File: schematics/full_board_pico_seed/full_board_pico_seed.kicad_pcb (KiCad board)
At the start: 4 copper layers, 128.3 x 74.9 mm, 135 parts, among them J1 XLR3, J10 Conn_02x20_Odd_Even, J2 Conn_01x02_Male, J3 Aux In, J4 Conn_01x02_Pin, J5 Conn_02x03_Odd_Even, J6 Conn_01x03_Female, J7 XLR3, J8 XLR3, J9 Conn_01x03, P0 25k, P1 25k, P2 25k, SW1 Stompbutton 1, SW2 Stompbutton 2, SW3 Stompbutton 3, SW4 Enter, SW5 Exit, U10 LM4881M/NOPB, U12 128X64 OLED Display, U14 AP63205WU, U2 PCM3060PWR, U3 LM1117DT-5.0, U4 OPA134, U5 ATmega88A-A, U6 24LC128, U7 OPA2342, U9 OPA4342, X1 SG-5032CAN

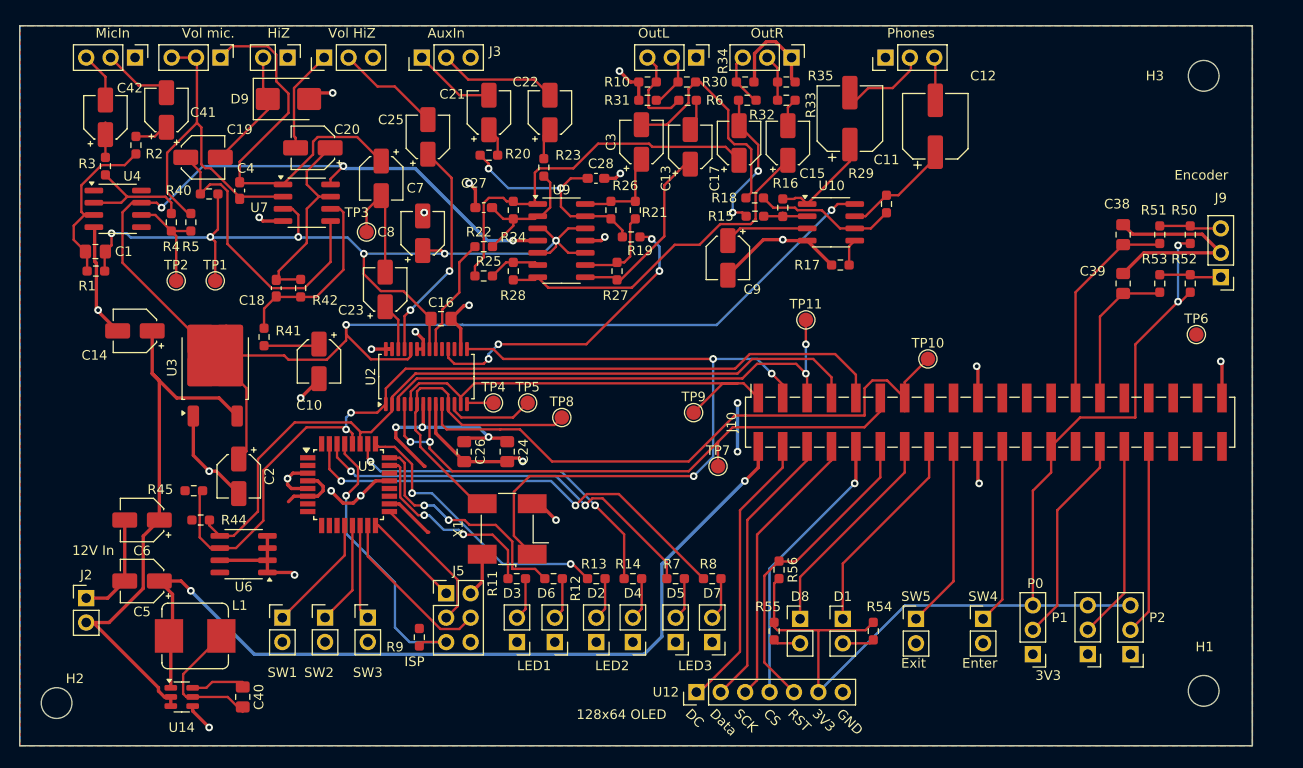
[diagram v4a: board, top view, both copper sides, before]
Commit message: added a few testpoints
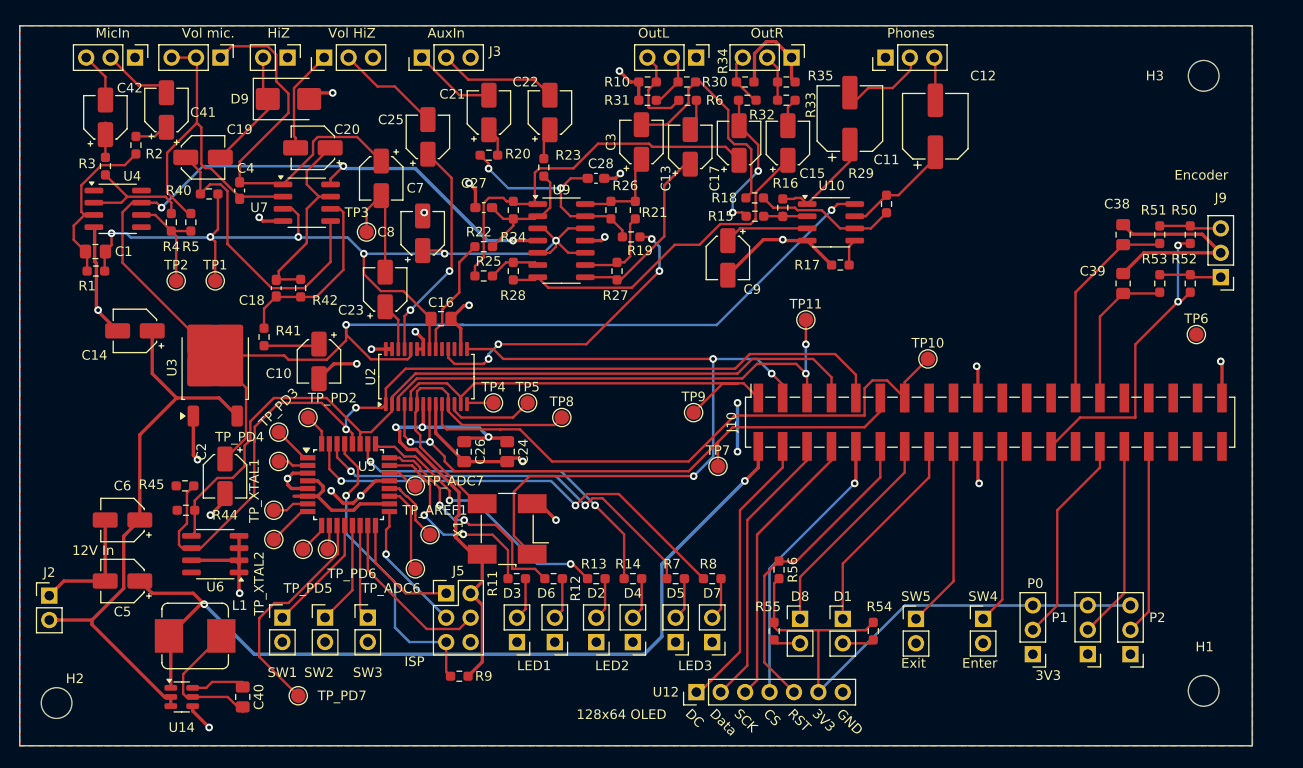
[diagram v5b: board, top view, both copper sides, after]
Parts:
- added TP_ADC6: ~, TestPoint:TestPoint_Pad_D1.5mm, F.Cu at (111.0, 119.4)
- added TP_ADC7: ~, TestPoint:TestPoint_Pad_D1.5mm, F.Cu at (111.0, 110.7)
- added TP_AREF1: ~, TestPoint:TestPoint_Pad_D1.5mm, F.Cu at (112.5, 115.8)
- added TP_PD2: ~, TestPoint:TestPoint_Pad_D1.5mm, F.Cu at (99.8, 103.6)
- added TP_PD3: ~, TestPoint:TestPoint_Pad_D1.5mm, F.Cu at (96.8, 105.2)
- added TP_PD4: ~, TestPoint:TestPoint_Pad_D1.5mm, F.Cu at (96.8, 108.2)
- added TP_PD5: ~, TestPoint:TestPoint_Pad_D1.5mm, F.Cu at (99.3, 117.3)
- added TP_PD6: ~, TestPoint:TestPoint_Pad_D1.5mm, F.Cu at (101.9, 117.3)
- added TP_PD7: ~, TestPoint:TestPoint_Pad_D1.5mm, F.Cu at (98.8, 132.6)
- added TP_XTAL1: TestPoint, TestPoint:TestPoint_Pad_D1.5mm, F.Cu at (96.3, 113.3)
- added TP_XTAL2: TestPoint, TestPoint:TestPoint_Pad_D1.5mm, F.Cu at (96.3, 116.3)
- moved R9 5.81 mm to (115.6, 130.6), turned to 180 degrees
- moved J2 3.85 mm to (72.9, 122.2)
- moved U6 2.95 mm to (90.2, 117.9)
- moved C5 2.03 mm to (80.5, 120.7)
- moved C6 2.03 mm to (80.5, 114.3)
- moved R44 1.84 mm to (87.1, 113.3)
- moved C2 1.43 mm to (91.2, 109.8)
- moved R45 1.05 mm to (87.0, 110.7)
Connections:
- U5 pad 1: unconnected-(U5-PD3-Pad1) -> Net-(U5-PD3)
- U5 pad 10: unconnected-(U5-PD6-Pad10) -> Net-(U5-PD6)
- U5 pad 11: unconnected-(U5-PD7-Pad11) -> Net-(U5-PD7)
- U5 pad 19: unconnected-(U5-ADC6-Pad19) -> Net-(U5-ADC6)
- U5 pad 2: unconnected-(U5-PD4-Pad2) -> Net-(U5-PD4)
- U5 pad 20: unconnected-(U5-AREF-Pad20) -> Net-(U5-AREF)
- U5 pad 22: unconnected-(U5-ADC7-Pad22) -> Net-(U5-ADC7)
- U5 pad 32: unconnected-(U5-PD2-Pad32) -> Net-(U5-PD2)
- U5 pad 7: unconnected-(U5-XTAL1/PB6-Pad7) -> Net-(U5-XTAL1/PB6)
- U5 pad 8: unconnected-(U5-XTAL2/PB7-Pad8) -> Net-(U5-XTAL2/PB7)
- U5 pad 9: unconnected-(U5-PD5-Pad9) -> Net-(U5-PD5)
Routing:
- net Net-(U5-PD7): track 0.00 -> 23.7 mm
- net Net-(U5-ADC6): track 0.00 -> 9.29 mm
- net 3V3: track 153.8 -> 161.3 mm
- net Net-(U5-AREF): track 0.00 -> 7.22 mm
- net /Codec/SCL: track 92.4 -> 99.2 mm
- net Net-(U5-XTAL2/PB7): track 0.00 -> 4.73 mm
- net Net-(U5-PD3): track 0.00 -> 4.24 mm
- net /Codec/SDA: track 82.5 -> 86.6 mm
- net Net-(U5-PD2): track 0.00 -> 3.33 mm
- net Net-(U5-XTAL1/PB6): track 0.00 -> 3.29 mm
- net Net-(U5-PD5): track 0.00 -> 3.28 mm
- net Net-(U5-PD4): track 0.00 -> 3.19 mm
- net Net-(U5-ADC7): track 0.00 -> 2.67 mm
- net Net-(U5-PD6): track 0.00 -> 2.55 mm
- net Net-(J5-Pin_1): track 10.8 -> 13.1 mm
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
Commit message: kicad version update/grade
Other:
- board text added: "PiPicoFX Full Board V0.1.0"

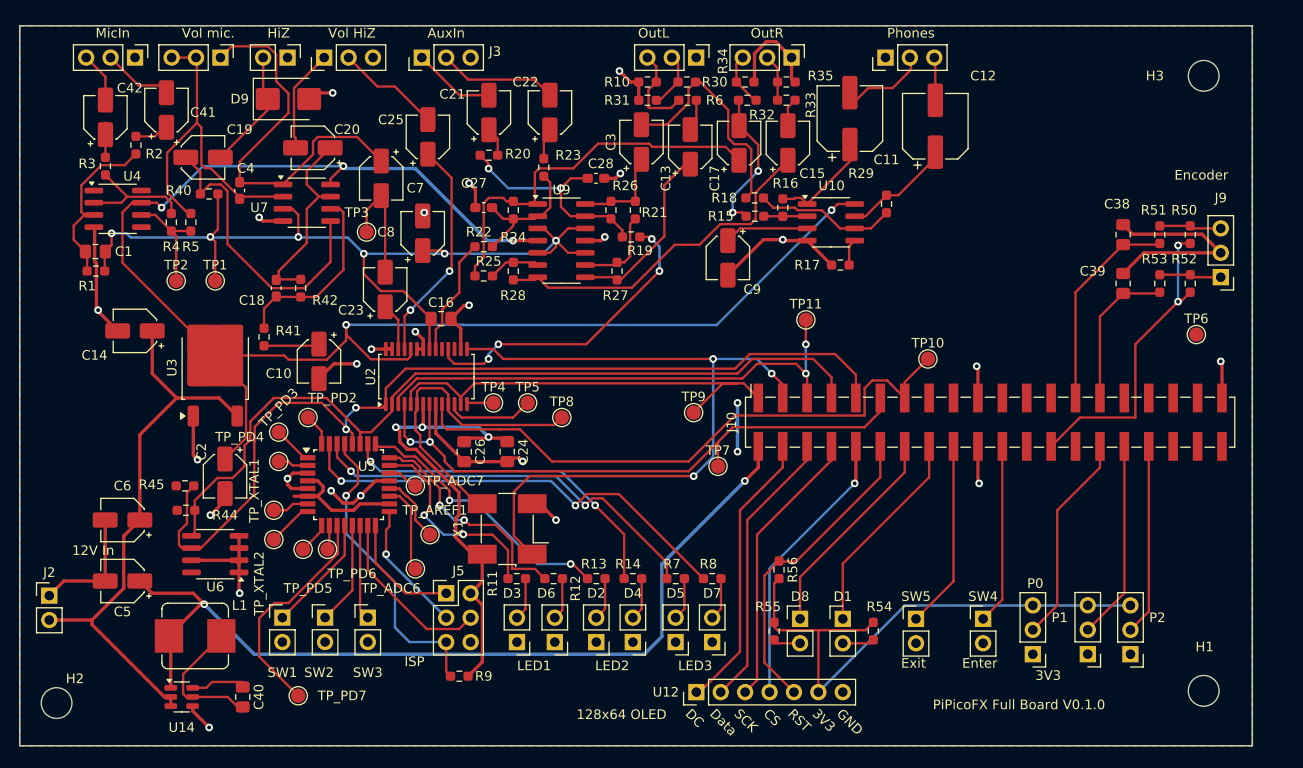
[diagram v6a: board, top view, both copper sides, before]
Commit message: corrected wiring mistake found during hw test of first batch
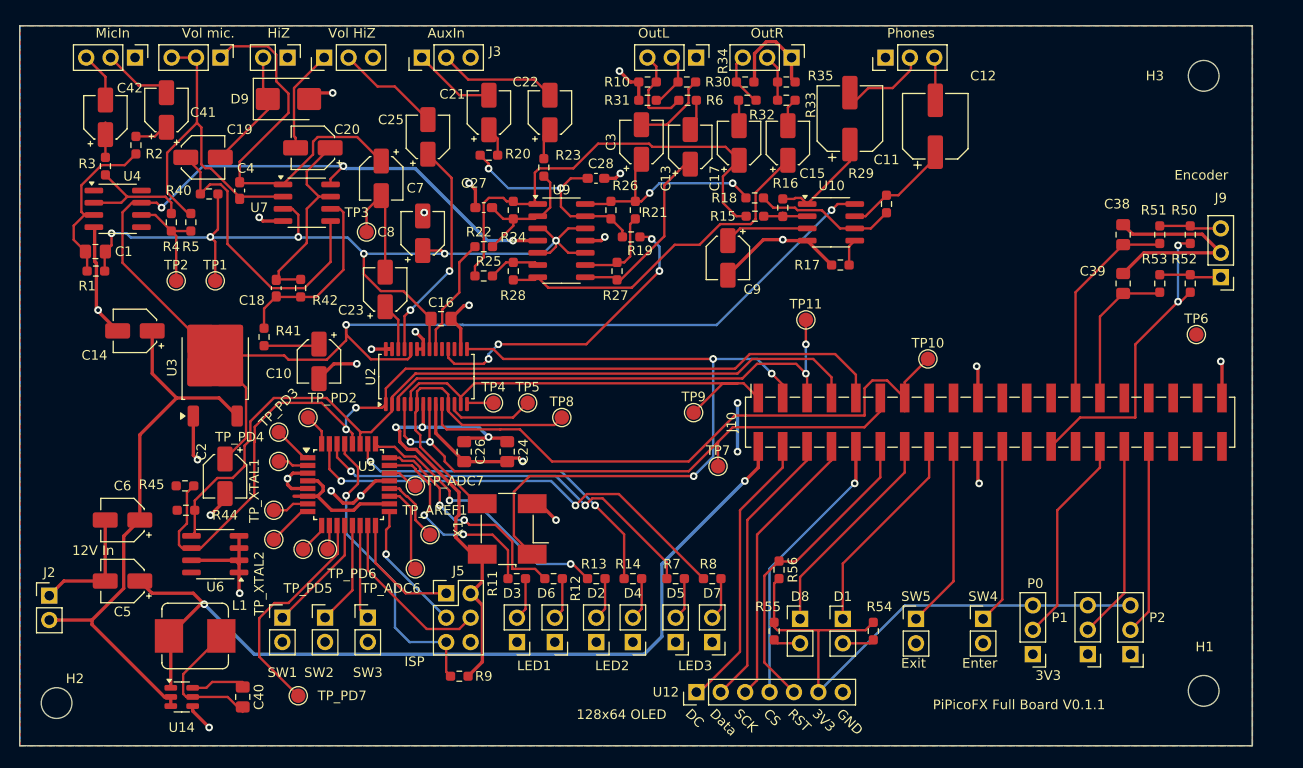
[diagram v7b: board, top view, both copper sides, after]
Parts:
- C16: value 0.1u -> 0.1uF
- C2: value 56uF -> 22uF
- C8: value 10u -> 10uF
- X1: value SG-5032CAN -> SG-5032CAN 12.288MHz
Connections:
- C17 pad 1: Net-(C17-Pad1) -> /Analog Preamp/Left Analog Out
- C17 pad 2: /Analog Preamp/Left Analog Out -> Net-(C17-Pad2)
- C3 pad 1: Net-(C3-Pad1) -> /Analog Preamp/Right Analog Out
- C3 pad 2: /Analog Preamp/Right Analog Out -> Net-(C3-Pad2)
- R21 pad 1: Net-(C3-Pad1) -> /Analog Preamp/Right Analog Out
- R24 pad 2: Net-(C17-Pad1) -> /Analog Preamp/Left Analog Out
- R25 pad 1: Net-(C17-Pad1) -> /Analog Preamp/Left Analog Out
- R26 pad 2: Net-(C3-Pad1) -> /Analog Preamp/Right Analog Out
- R30 pad 1: /Analog Preamp/Right Analog Out -> Net-(C3-Pad2)
- R32 pad 1: /Analog Preamp/Left Analog Out -> Net-(C17-Pad2)
- U9 pad 1: Net-(C17-Pad1) -> /Analog Preamp/Left Analog Out
- U9 pad 14: Net-(C3-Pad1) -> /Analog Preamp/Right Analog Out
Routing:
- net Net-(C17-Pad1): track 40.7 -> 0.00 mm
- net /Analog Preamp/Left Analog Out: track 15.2 -> 48.8 mm, vias 2 -> 0
- net Net-(C3-Pad1): track 9.97 -> 0.00 mm
- net Net-(C3-Pad2): track 0.00 -> 8.33 mm
- net Net-(C17-Pad2): track 0.00 -> 2.67 mm
- net /Analog Preamp/Right Analog Out: track 24.0 -> 23.0 mm, vias 0 -> 2
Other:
- board text added: "PiPicoFX Full Board V0.1.1"
- board text removed: "PiPicoFX Full Board V0.1.0"

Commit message: corrected schematic regarding pcm3060
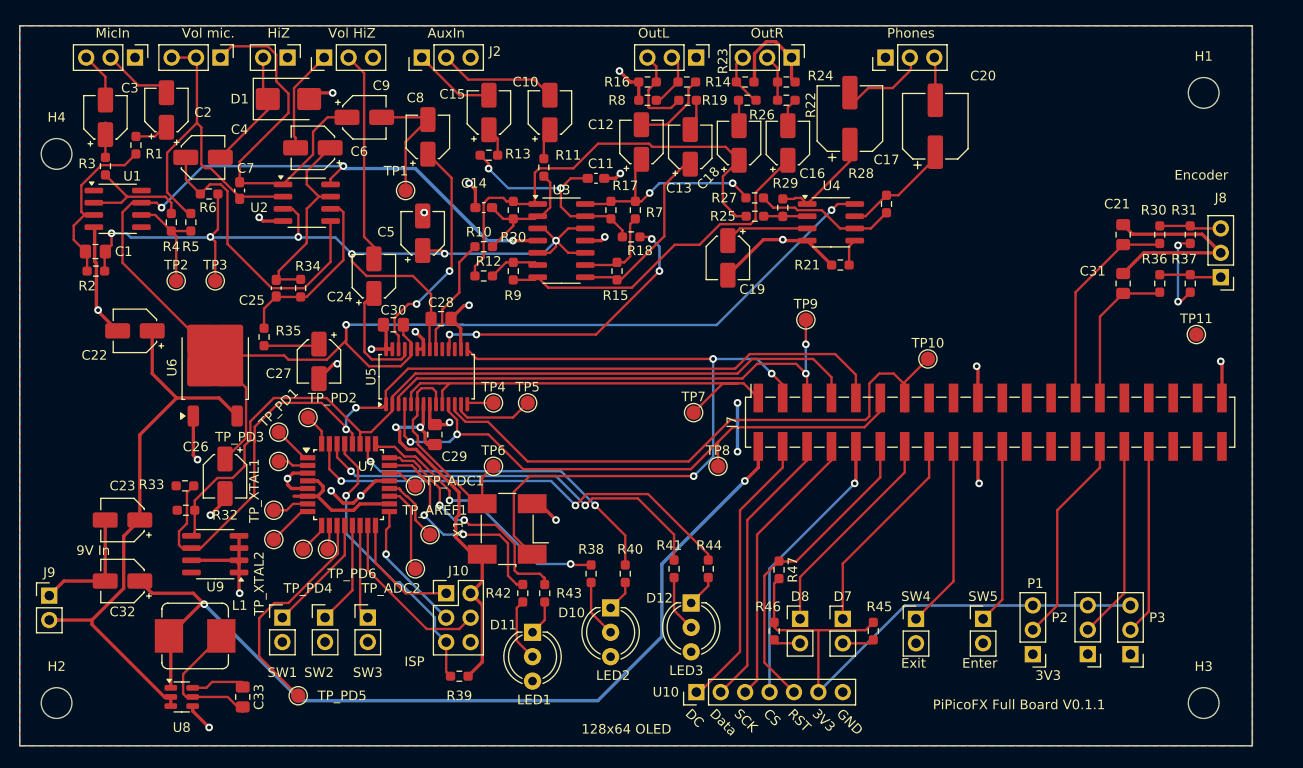
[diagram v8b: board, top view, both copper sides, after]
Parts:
- removed D2, D3, D4, D5, D6: LED, Connector_PinHeader_2.54mm:PinHeader_1x02_P2.54mm_Vertical
- removed the D7 at (141.9, 127.0)
- removed the U2 at (112.1, 99.4)
- added D10: LED_Dual_AAK, LED_THT:LED_D5.0mm-3, F.Cu at (131.3, 123.4)
- added D11: LED_Dual_AAK, LED_THT:LED_D5.0mm-3, F.Cu at (123.2, 126.0)
- added D12: LED_Dual_AAK, LED_THT:LED_D5.0mm-3, F.Cu at (139.7, 122.9)
- added H4: MountingHole, MountingHole:MountingHole_3.2mm_M3, F.Cu at (73.7, 76.2)
- added U5: PCM3060, Package_SO:TSSOP-28_4.4x9.7mm_P0.65mm, F.Cu at (112.2, 99.4)
- RV2: value 10k -> 50k
- moved C30 17.7 mm to (108.7, 94.0), turned to 180 degrees
- moved TP6 8.74 mm to (119.1, 108.7)
- moved C9 6.59 mm to (105.7, 72.4), turned to 0 degrees
- moved TP1 5.93 mm to (110.0, 80.0)
- moved C29 3.53 mm to (113.0, 105.4), turned to 90 degrees
- moved C24 1.81 mm to (106.7, 88.9)
- moved H1 1.78 mm to (193.0, 69.8)
- moved R43 1.78 mm to (124.5, 121.9), turned to 90 degrees
- moved R42 1.64 mm to (122.2, 121.9), turned to 90 degrees
- moved H3 1.27 mm to (193.0, 133.3)
- moved R44 1.10 mm to (141.5, 119.4), turned to 90 degrees
- moved R41 1.03 mm to (137.9, 119.4), turned to 90 degrees
- moved R40 0.95 mm to (132.8, 119.9), turned to 90 degrees
- moved R38 0.75 mm to (129.3, 119.9), turned to 90 degrees
- renumbered C22 to C10, C28 to C11, C3 to C12, C27 to C14, C21 to C15, C15 to C16, C11 to C17, C17 to C18, C9 to C19, C41 to C2, C12 to C20, C38 to C21, C14 to C22, C6 to C23, C23 to C24, C18 to C25, C2 to C26, C10 to C27, C16 to C28, C26 to C29, C42 to C3, C24 to C30, C39 to C31, C5 to C32, C40 to C33, C19 to C4, C8 to C5, C20 to C6, C4 to C7, C25 to C8, C7 to C9, D9 to D1, D1 to D7, H3 to H1, H1 to H3, J5 to J10, J3 to J2, J4 to J3, J6 to J4, J8 to J5, J7 to J6, J10 to J7, J9 to J8, J2 to J9, P0 to P1, P1 to P2, P2 to P3, R2 to R1, R22 to R10, R23 to R11, R25 to R12, R20 to R13, R30 to R14, R27 to R15, R10 to R16, R26 to R17, R19 to R18, R6 to R19, R1 to R2, R24 to R20, R17 to R21, R33 to R22, R34 to R23, R35 to R24, R15 to R25, R32 to R26, R18 to R27, R29 to R28, R16 to R29, R51 to R30, R50 to R31, R44 to R32, R45 to R33, R42 to R34, R41 to R35, R53 to R36, R52 to R37, R13 to R38, R9 to R39, R14 to R40, R7 to R41, R11 to R42, R12 to R43, R8 to R44, R54 to R45, R55 to R46, R56 to R47, R40 to R6, R21 to R7, R31 to R8, R28 to R9, SW5 to SW4, SW4 to SW5, TP3 to TP1, TP6 to TP11, TP1 to TP3, TP8 to TP6, TP9 to TP7, TP7 to TP8, TP11 to TP9, TP_ADC7 to TP_ADC1, TP_ADC6 to TP_ADC2, TP_PD3 to TP_PD1, TP_PD4 to TP_PD3, TP_PD5 to TP_PD4, TP_PD7 to TP_PD5, U4 to U1, U12 to U10, U7 to U2, U9 to U3, U10 to U4, U3 to U6, U5 to U7, U14 to U8, U6 to U9
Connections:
- C24 pad 2: /Analog Preamp/Mic -> /Analog Preamp/HiZ
- C30 pad 1: 3V3 -> 5V
- C8 pad 2: /Analog Preamp/HiZ -> /Analog Preamp/Mic
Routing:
- net 3V3: track 161.3 -> 128.1 mm, vias 7 -> 6
- net /Analog Preamp/HiZ: track 10.9 -> 21.5 mm
- net Net-(U5-SCKI1): track 33.6 -> 23.5 mm
- net GND: track 167.5 -> 158.5 mm
- net Net-(U5-V_{IN}L): track 4.97 -> 11.9 mm
- net 5V: track 165.0 -> 169.0 mm
- net 5V_DIG: track 93.4 -> 97.4 mm
- net Net-(C7-Pad2): track 41.6 -> 38.5 mm
- net Net-(D11-A2): track 4.43 -> 6.63 mm
- net Net-(U7-PC0): track 21.8 -> 23.8 mm
- net /Analog Preamp/VCom: track 95.6 -> 97.6 mm
- net Net-(J10-Pin_5): track 32.0 -> 30.1 mm
- net Net-(D10-A2): track 4.44 -> 6.03 mm
- net Net-(U7-PC3): track 36.1 -> 34.7 mm
- net /Analog Preamp/DacR+: track 32.4 -> 31.1 mm
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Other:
- board text added: "9V In"
- board text removed: "12V In"
